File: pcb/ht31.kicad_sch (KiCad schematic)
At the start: 7 parts, among them J5 I2C Board, J6 I2C Sensor, U3 SHT31-DIS

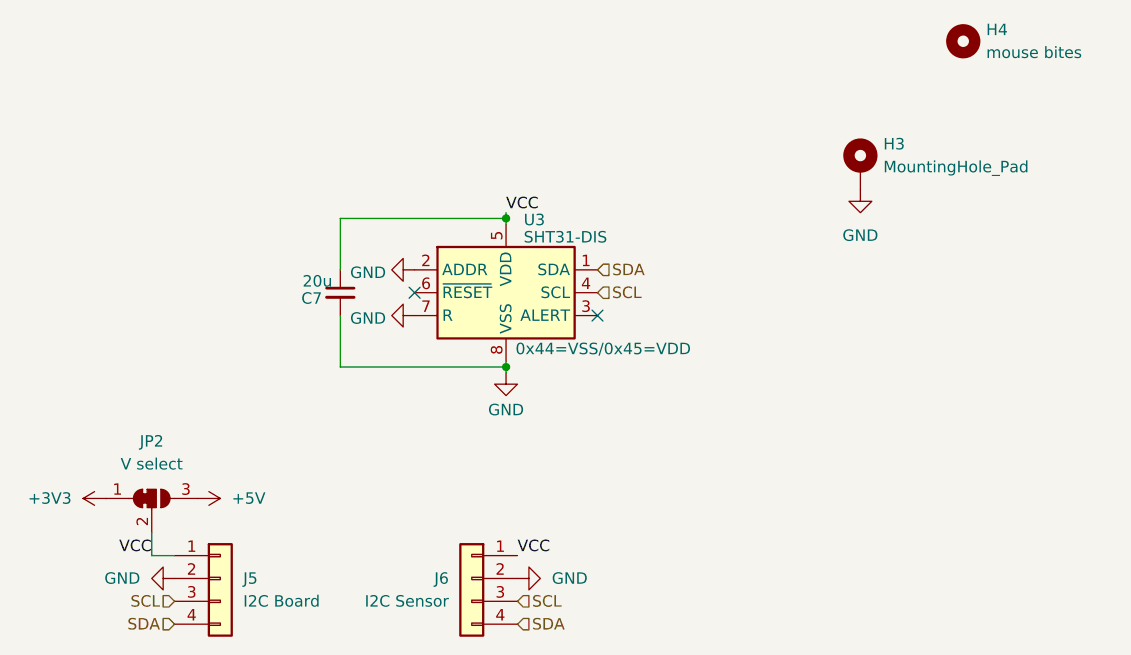
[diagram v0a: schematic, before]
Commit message: Rename pcb, add sensors and fix some issues
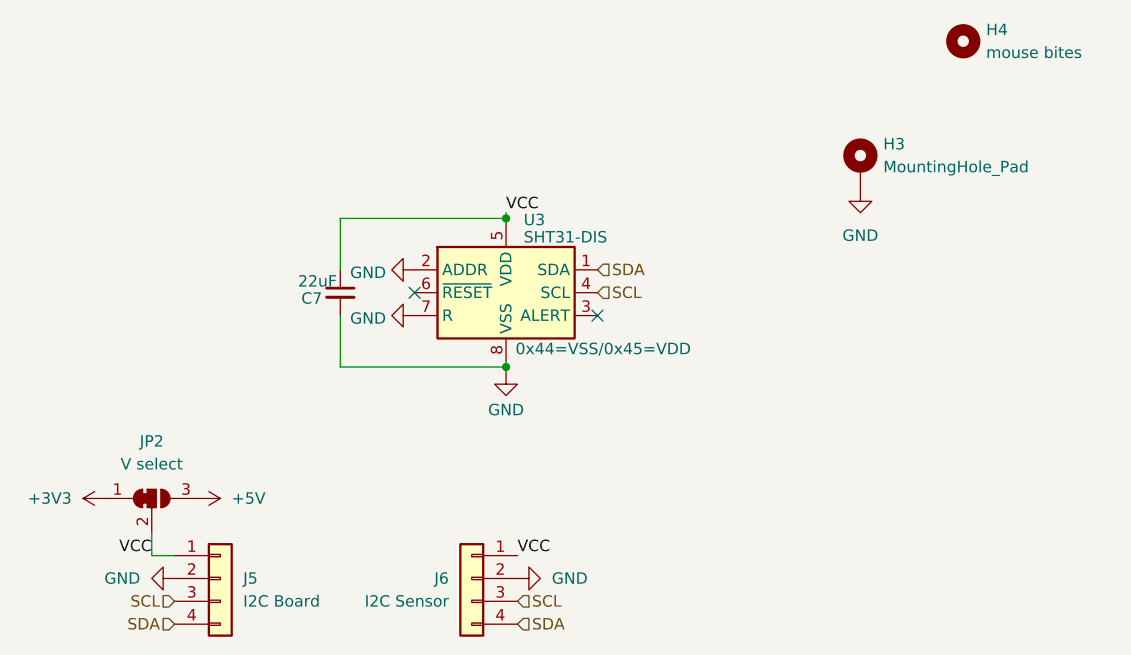
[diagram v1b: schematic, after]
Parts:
- C7: value 20u -> 22uF
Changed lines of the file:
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@@
 			)
 		)
-		(property "Value" "20u"
+		(property "Value" "22uF"
 			(at 55.245 71.12 0)
 			(effects
